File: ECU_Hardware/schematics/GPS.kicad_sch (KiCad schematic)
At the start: 1 part, among them U1 ATGM336H-5N31

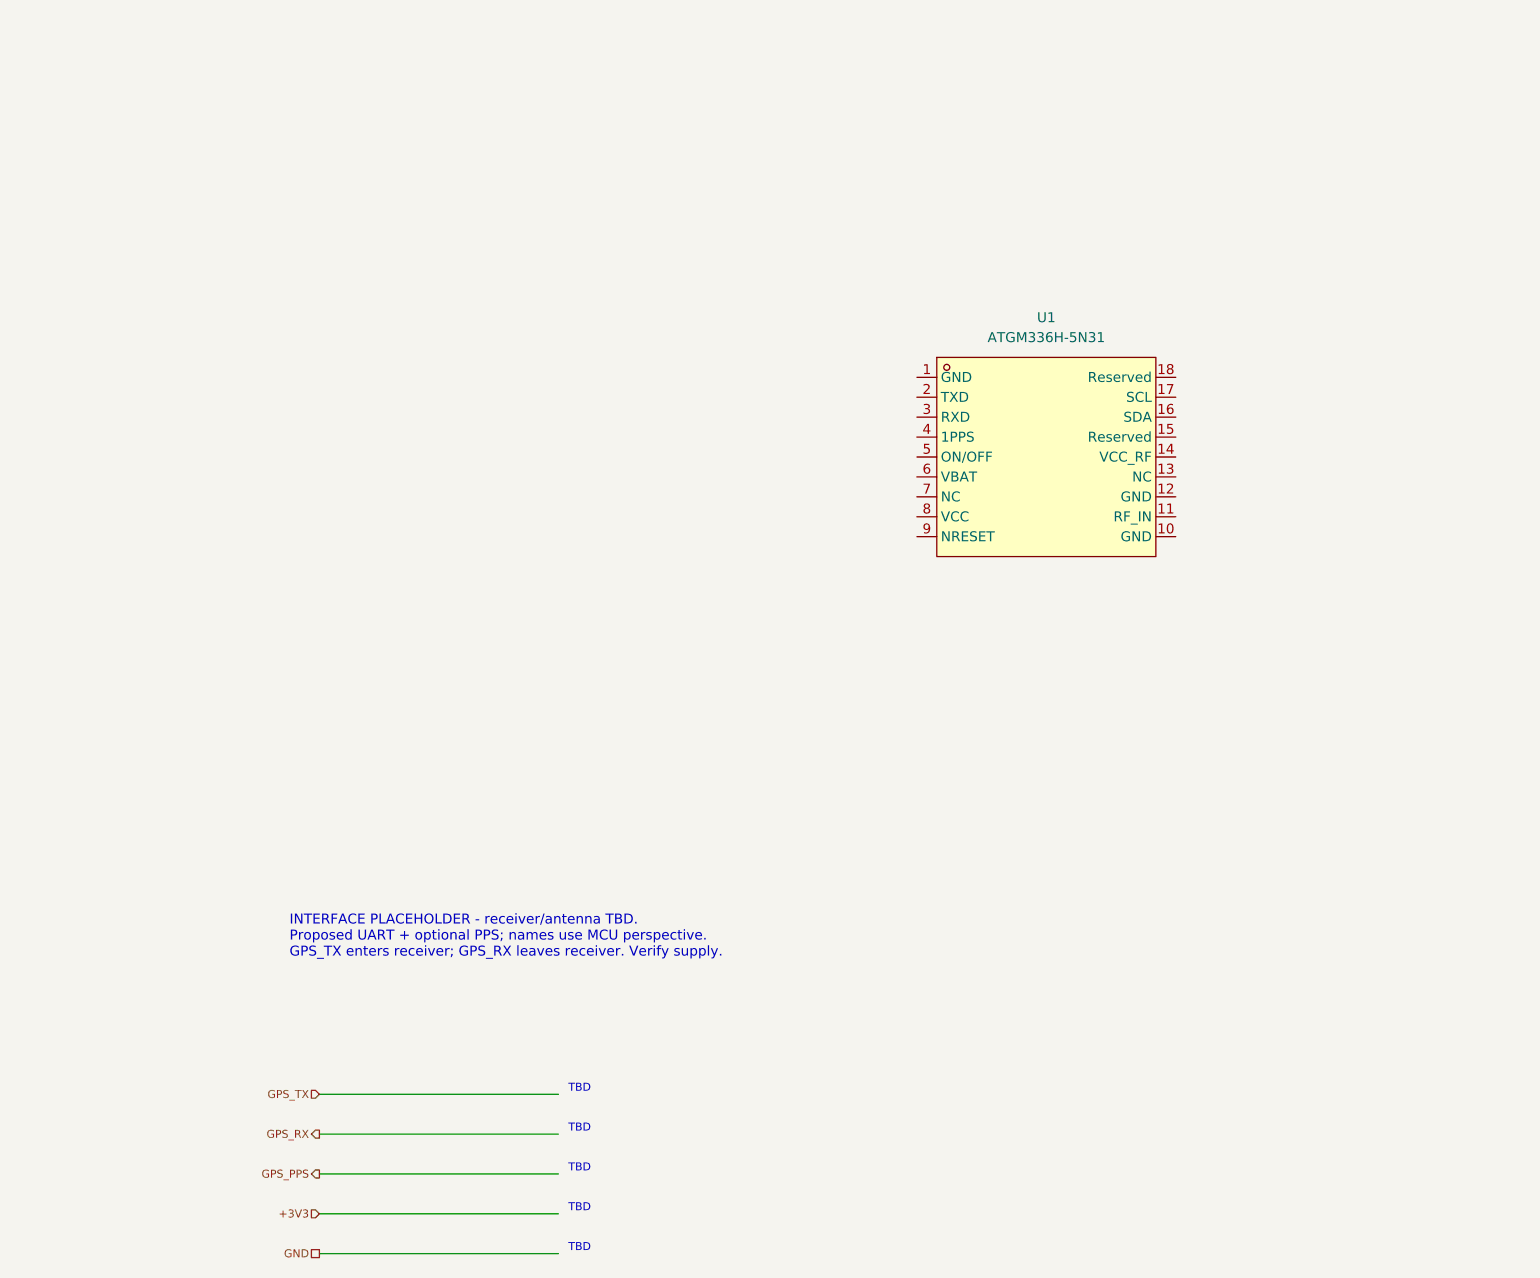
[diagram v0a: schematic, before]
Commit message: Move ECU schematics into schematics/ and add driver inputs and sensor notes
Hierarchical sheets now live in ECU_Hardware/schematics, with the new
Driver_Inputs sheet (APPS, BPPS and steering dividers and clamps), the
reviewed and JLCPCB project symbol libraries, new 3D models, and
SENSOR_INTERFACES.md with the GPS, IMU and temperature pin allocation.
The old top-level sheets and the restore backup are removed.

Claude-Session: https://claude.ai/code/session_0117trEbCv7z6CPYkN3K3GKQ
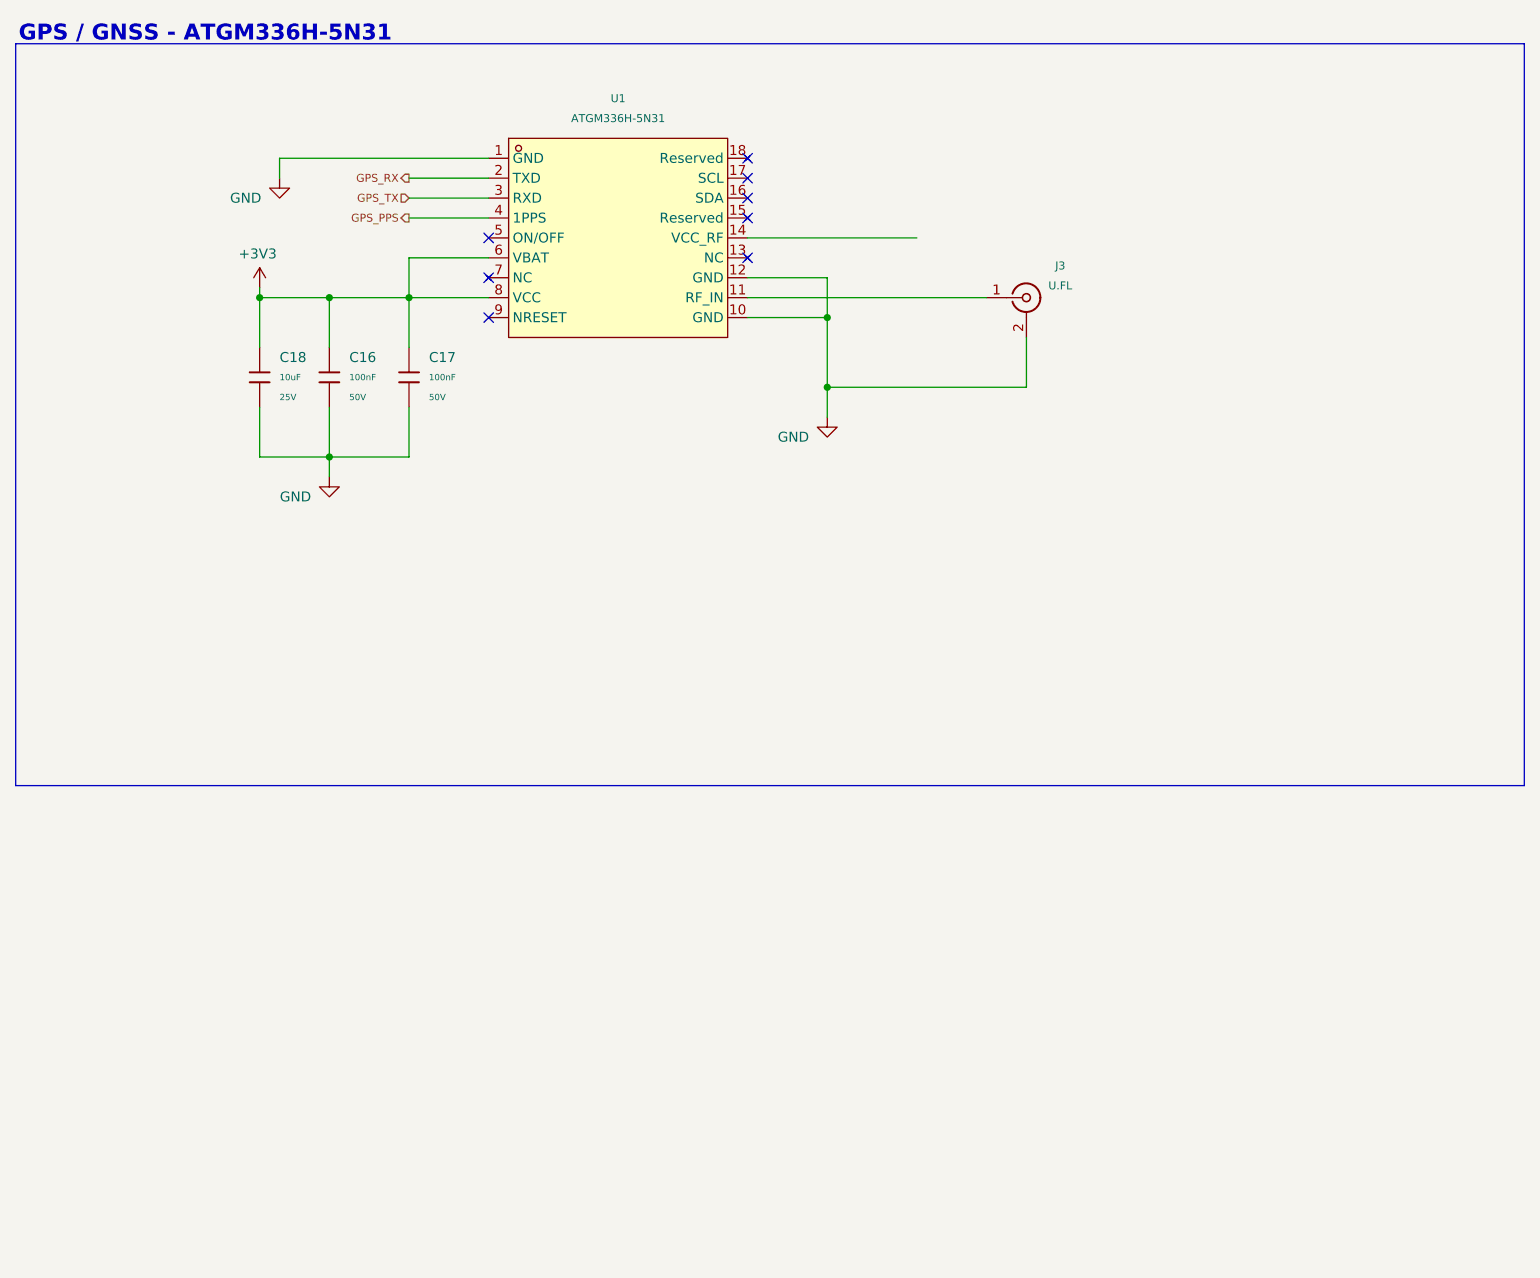
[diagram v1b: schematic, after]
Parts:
- added C16, C17: 100nF, PCM_JLCPCB:C_0402, symbol PCM_JLCPCB-Capacitors:0402,100nF,(2)
- added C18: 10uF, PCM_JLCPCB:C_0603, symbol PCM_JLCPCB-Capacitors:0603,10uF,(2)
- added J3: U.FL, PCM_JLCPCB:IPEX-SMD_BWIPX-1-001E, symbol ECU_Reviewed:RF, Connector, U.FL
- U1: symbol easyeda2kicad:ATGM336H-5N31 -> ECU_Reviewed:ATGM336H-5N31
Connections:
- net +3V3: now also U1.6 (VBAT), U1.8 (VCC), C16.1, C17.1, C18.1
- net GND: now also U1.1 (GND), U1.10 (GND), U1.12 (GND), C16.2, C17.2, C18.2, J3.2 (Ext)
- net GPS_PPS: now also U1.4 (1PPS)
- net GPS_RX: now also U1.2 (TXD)
- net GPS_TX: now also U1.3 (RXD)
- net at U1.11 (RF_IN): now also J3.1 (In)
- no-connect marks 0 -> 8
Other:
- note added: "GPS / GNSS - ATGM336H-5N31"
- note removed: "INTERFACE PLACEHOLDER - receiver/antenna TBD. Proposed UART + optional PPS; names use MCU perspective. GPS_TX enters receiver; GPS_RX leaves receiver. Verify supply."
- note removed: "TBD"
